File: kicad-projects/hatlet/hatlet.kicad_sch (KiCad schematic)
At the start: 46 parts, among them J1 USB Header, J2 SWD, J3 PMOD0, J4 PMOD2, J5 PMOD1, J6 UART0, J7 PMOD3, SW1 BOOTSEL, U1 AMS1117-3.3, U2 RP2040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

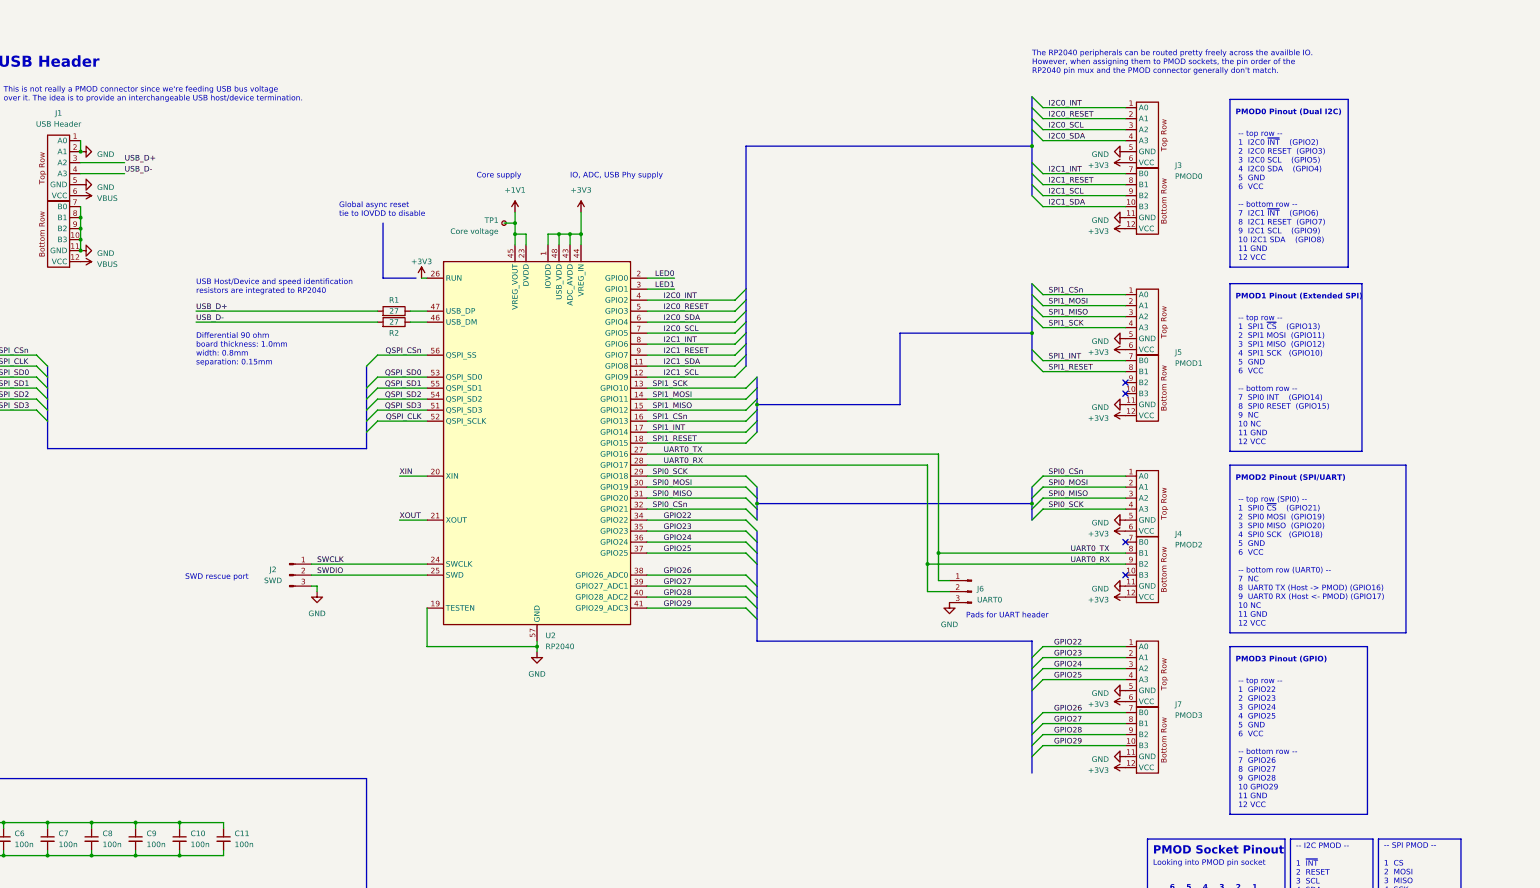
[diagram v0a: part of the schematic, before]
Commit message: Finish hatlet rev A layout
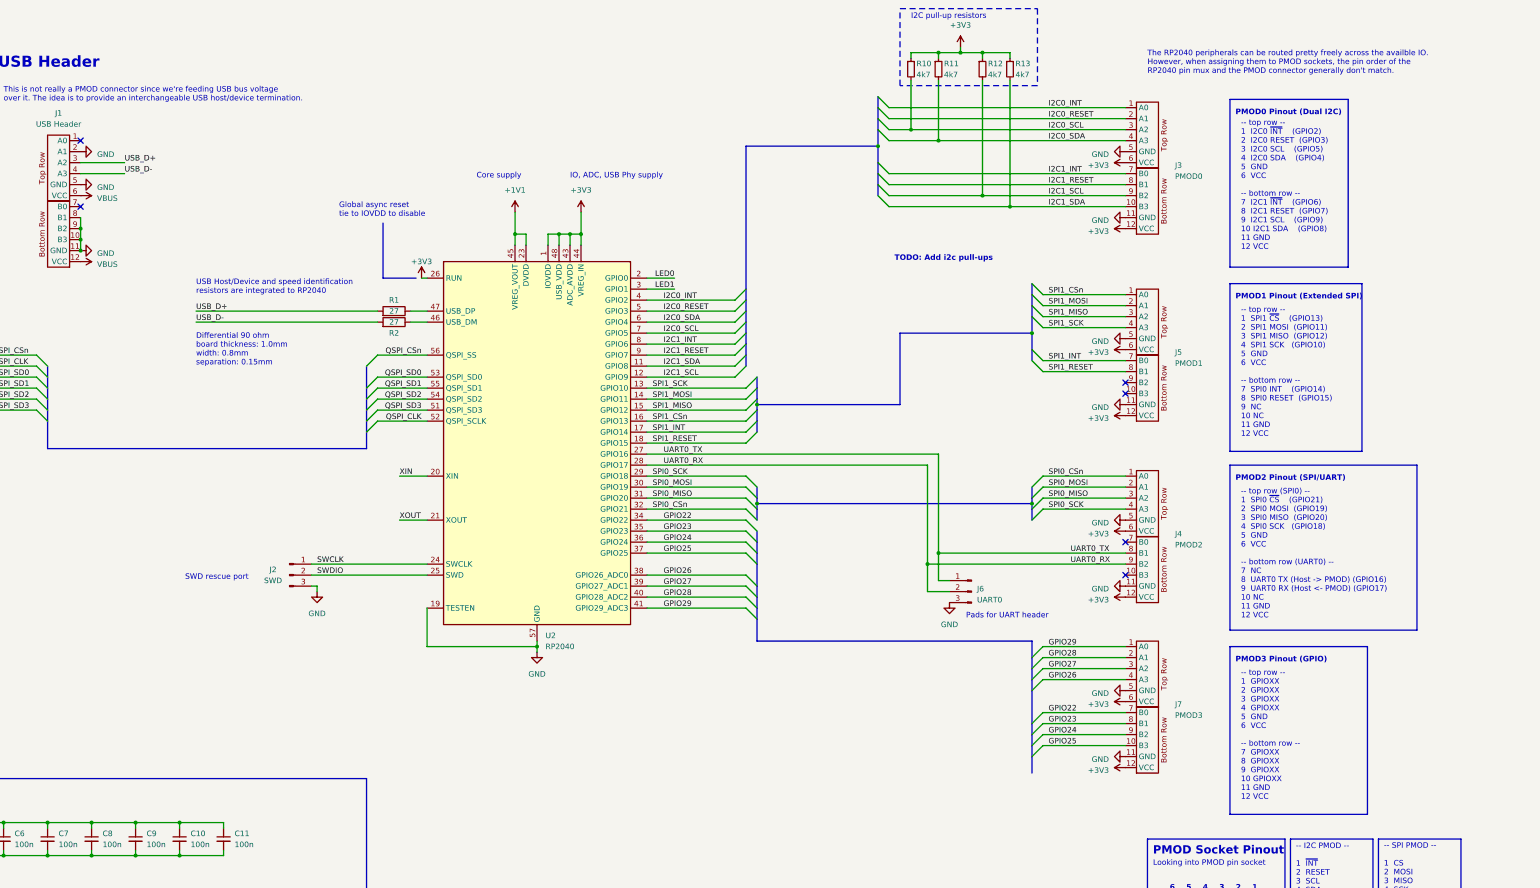
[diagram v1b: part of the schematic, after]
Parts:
- removed TP1: Core voltage, TestPoint:TestPoint_Pad_D1.0mm, symbol Connector:TestPoint_Small
- added R10, R11, R12, R13: 4k7, Resistor_SMD:R_0603_1608Metric, symbol Device:R_Small
- D1, D2, D3, D4: footprint LED_SMD:LED_0603_1608Metric -> LED_SMD:LED_0805_2012Metric
- J2, J6: footprint Connector_PinHeader_2.54mm:PinHeader_1x03_P2.54mm_Vertical -> Connector_PinHeader_2.54mm:PinHeader_1x03_P2.54mm_Horizontal
- U2: footprint Package_DFN_QFN:QFN-56-1EP_7x7mm_P0.4mm_EP3.2x3.2mm -> Package_DFN_QFN:QFN-56-1EP_7x7mm_P0.4mm_EP3.2x3.2mm_ThermalVias
- U3: footprint Package_SO:SOIC-8_5.23x5.23mm_P1.27mm -> Package_SO:SOIC-8_5.275x5.275mm_P1.27mm; lcsc (none) -> https://www.lcsc.com/product-detail/NOR-FLASH_Winbond-Elec-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
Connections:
- net +3V3: now also R10.1, R11.1, R12.1, R13.1
- net GND: no longer J1.1 (A0), J1.7 (B0)
- net GPIO22: now also J7.7 (B0); no longer J7.1 (A0)
- net GPIO23: now also J7.8 (B1); no longer J7.2 (A1)
- net GPIO24: now also J7.9 (B2); no longer J7.3 (A2)
- net GPIO25: now also J7.10 (B3); no longer J7.4 (A3)
- net GPIO26: now also J7.4 (A3); no longer J7.7 (B0)
- net GPIO27: now also J7.3 (A2); no longer J7.8 (B1)
- net GPIO28: now also J7.2 (A1); no longer J7.9 (B2)
- net GPIO29: now also J7.1 (A0); no longer J7.10 (B3)
- net I2C0_SCL: now also R10.2
- net I2C0_SDA: now also R11.2
- net I2C1_SCL: now also R12.2
- net I2C1_SDA: now also R13.2
- no-connect marks 4 -> 6
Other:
- note added: "-- top row -- 1 GPIOXX 2 GPIOXX 3 GPIOXX 4 GPIOXX 5 GND 6 VCC -- bottom row -- 7 GPIOXX 8 GPIOXX 9 GPIOXX 10 GPIOXX 11 GND 12 VCC"
- note added: "I2C pull-up resistors"
- note added: "TODO: Add i2c pull-ups"
- note removed: "-- top row -- 1 GPIO22 2 GPIO23 3 GPIO24 4 GPIO25 5 GND 6 VCC -- bottom row -- 7 GPIO26 8 GPIO27 9 GPIO28 10 GPIO29 11 GND 12 VCC"

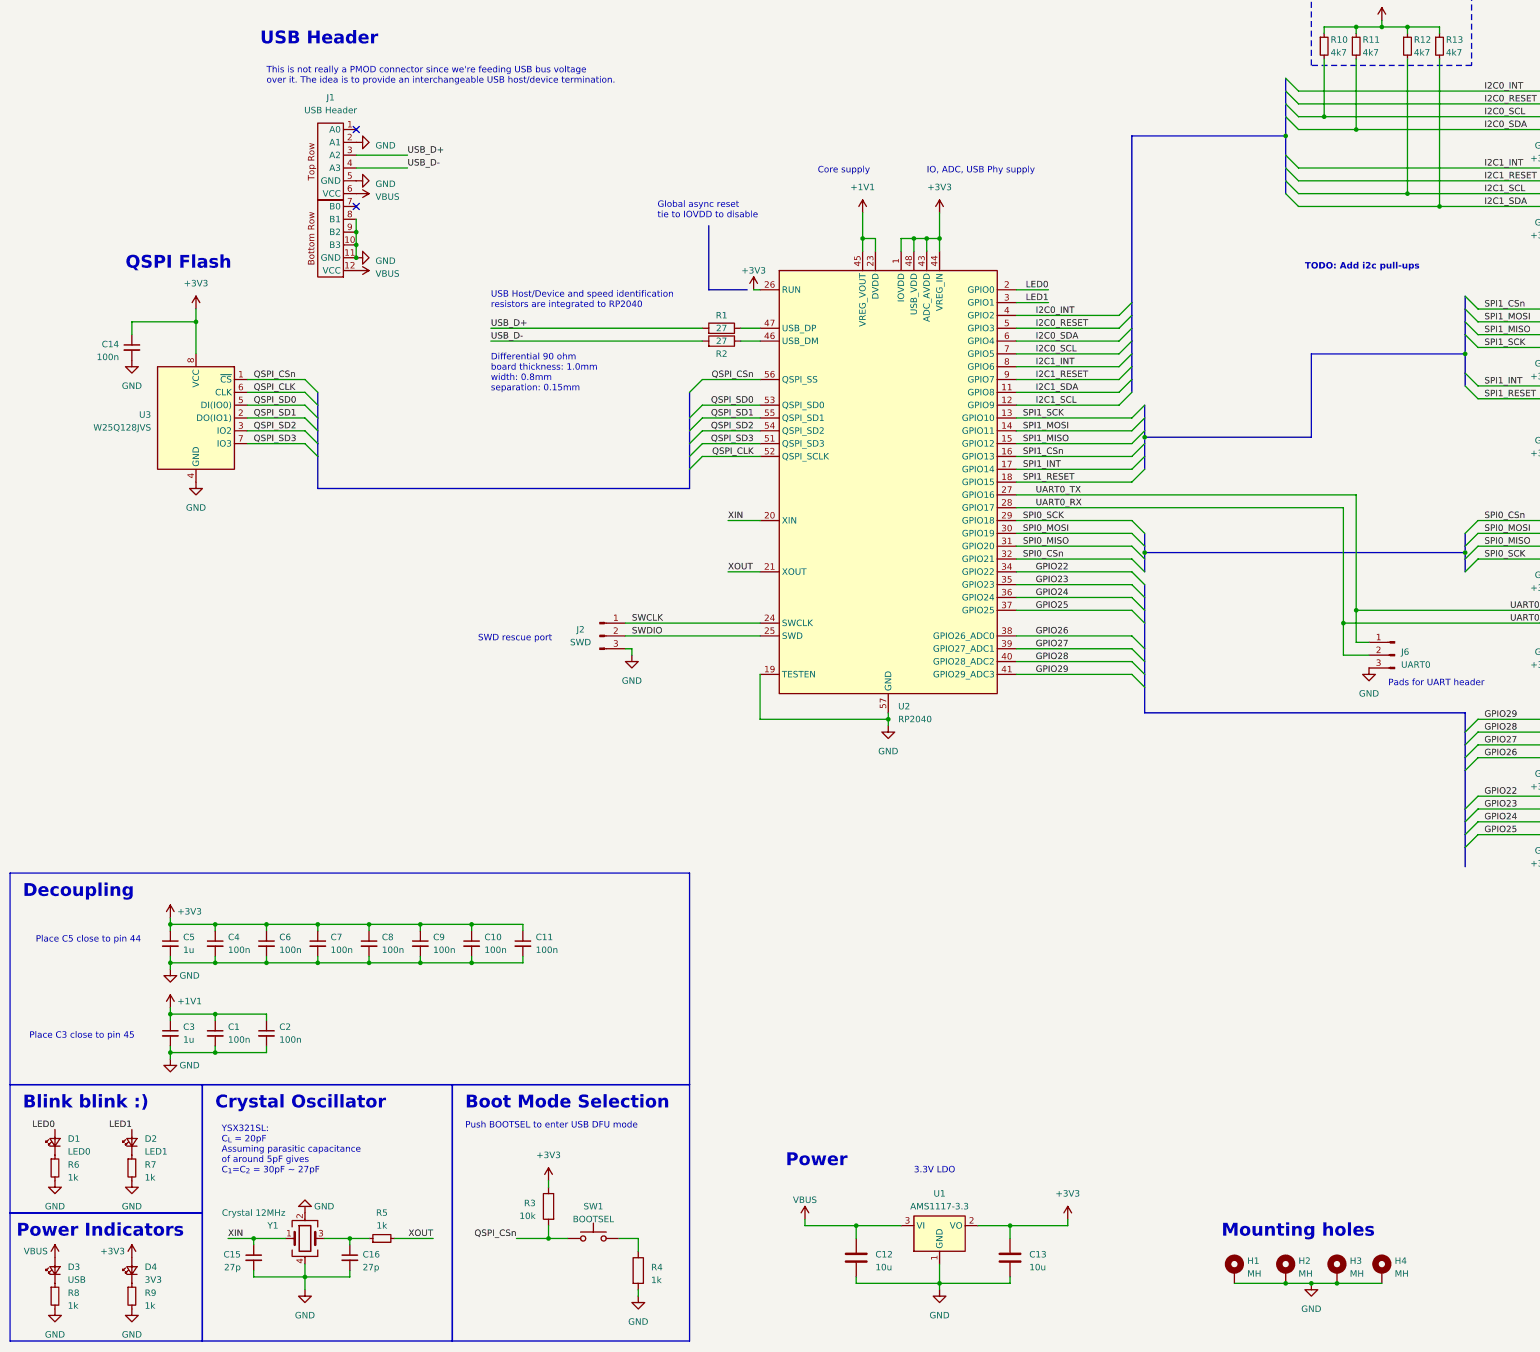
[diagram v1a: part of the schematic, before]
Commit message: Update USB header footprint
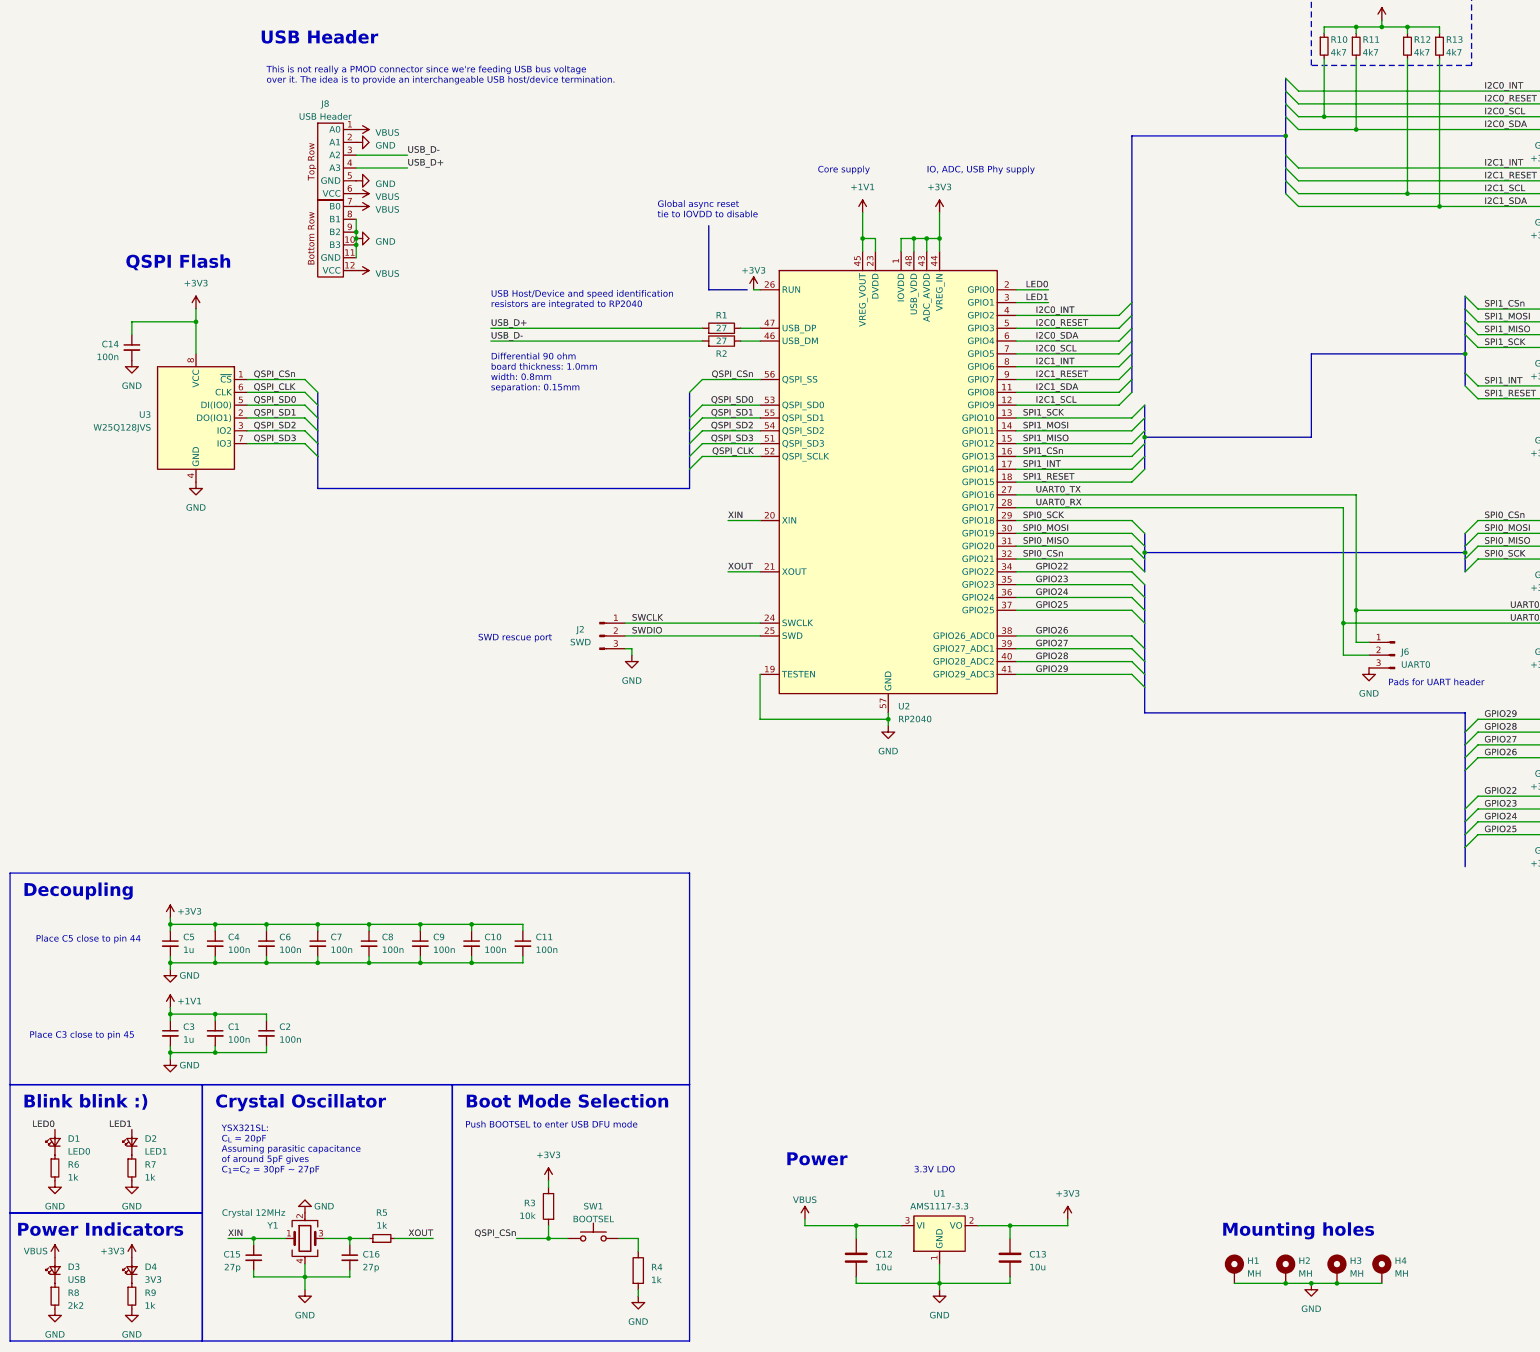
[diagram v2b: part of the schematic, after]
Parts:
- removed J1: USB Header, pmod:PMOD_PinSocket_2x06_P2.54mm_Horizontal, symbol pmod:PMOD_Host_Conn_02x06
- added J8: USB Header, racklet:Racklet_USBHeader_02x06, symbol pmod:PMOD_Peripheral_Conn_02x06
- C1, C10, C11, C14, C2, C4, C6, C7, C8, C9: JLCPCB Part # (none) -> C14663
- C12, C13: JLCPCB Part # (none) -> C96446
- C15, C16: JLCPCB Part # (none) -> C107045
- C3, C5: JLCPCB Part # (none) -> C15849
- D1, D2, D3, D4: JLCPCB Part # (none) -> C84256
- R1, R2: JLCPCB Part # (none) -> C25190
- R10, R11, R12, R13: JLCPCB Part # (none) -> C23162
- R3: JLCPCB Part # (none) -> C25804
- R4, R5, R6, R7, R9: JLCPCB Part # (none) -> C21190
- R8: value 1k -> 2k2; JLCPCB Part # (none) -> C4190
- SW1: footprint Button_Switch_SMD:SW_SPST_SKQG_WithStem -> Button_Switch_SMD:SW_SPST_TL3342; JLCPCB Part # (none) -> C318884
- U1: JLCPCB Part # (none) -> C6186
- U2: JLCPCB Part # (none) -> C2040
- U3: JLCPCB Part # (none) -> C97521
- Y1: JLCPCB Part # (none) -> C9002
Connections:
- net GND: now also J8.10 (B3), J8.11 (GND), J8.2 (A1), J8.5 (GND), J8.8 (B1), J8.9 (B2)
- net USB_D+: now also J8.4 (A3)
- net USB_D-: now also J8.3 (A2)
- net VBUS: now also J8.1 (A0), J8.12 (VCC), J8.6 (VCC), J8.7 (B0)
- no-connect marks 6 -> 4
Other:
- note removed: "TODO: Add i2c pull-ups"

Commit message: Rename schematic LCSC designator field
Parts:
- C1, C10, C11, C14, C2, C4, C6, C7, C8, C9: JLCPCB Part # C14663 -> (none); LCSC Part # (none) -> C14663
- C12, C13: JLCPCB Part # C96446 -> (none); LCSC Part # (none) -> C96446
- C15, C16: JLCPCB Part # C107045 -> (none); LCSC Part # (none) -> C107045
- C3, C5: JLCPCB Part # C15849 -> (none); LCSC Part # (none) -> C15849
- D1, D2, D3, D4: JLCPCB Part # C84256 -> (none); LCSC Part # (none) -> C84256
- R1, R2: JLCPCB Part # C25190 -> (none); LCSC Part # (none) -> C25190
- R10, R11, R12, R13: JLCPCB Part # C23162 -> (none); LCSC Part # (none) -> C23162
- R3: JLCPCB Part # C25804 -> (none); LCSC Part # (none) -> C25804
- R4, R5, R6, R7, R9: JLCPCB Part # C21190 -> (none); LCSC Part # (none) -> C21190
- R8: JLCPCB Part # C4190 -> (none); LCSC Part # (none) -> C4190
- SW1: JLCPCB Part # C318884 -> (none); LCSC Part # (none) -> C318884; lcsc https://www.lcsc.com/product-detail/Tactile-Switches_G-Swit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 -> (none)
- U1: JLCPCB Part # C6186 -> (none); LCSC Part # (none) -> C6186
- U2: JLCPCB Part # C2040 -> (none); LCSC Part # (none) -> C2040
- U3: JLCPCB Part # C97521 -> (none); LCSC Part # (none) -> C97521; lcsc https://www.lcsc.com/product-detail/NOR-FLASH_Winbond-Elec-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 -> (none)
- Y1: JLCPCB Part # C9002 -> (none); LCSC Part # (none) -> C9002; lcsc https://www.lcsc.com/product-detail/Crystals_Yangxing-Tech-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 -> (none)

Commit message: Revert "Rename schematic LCSC designator field"
This reverts commit 4d53cd782a2a552dfcb1ecbf5aa636fd93ad1774.
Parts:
- C1, C10, C11, C14, C2, C4, C6, C7, C8, C9: JLCPCB Part # (none) -> C14663; LCSC Part # C14663 -> (none)
- C12, C13: JLCPCB Part # (none) -> C96446; LCSC Part # C96446 -> (none)
- C15, C16: JLCPCB Part # (none) -> C107045; LCSC Part # C107045 -> (none)
- C3, C5: JLCPCB Part # (none) -> C15849; LCSC Part # C15849 -> (none)
- D1, D2, D3, D4: JLCPCB Part # (none) -> C84256; LCSC Part # C84256 -> (none)
- R1, R2: JLCPCB Part # (none) -> C25190; LCSC Part # C25190 -> (none)
- R10, R11, R12, R13: JLCPCB Part # (none) -> C23162; LCSC Part # C23162 -> (none)
- R3: JLCPCB Part # (none) -> C25804; LCSC Part # C25804 -> (none)
- R4, R5, R6, R7, R9: JLCPCB Part # (none) -> C21190; LCSC Part # C21190 -> (none)
- R8: JLCPCB Part # (none) -> C4190; LCSC Part # C4190 -> (none)
- SW1: JLCPCB Part # (none) -> C318884; LCSC Part # C318884 -> (none); lcsc (none) -> https://www.lcsc.com/product-detail/Tactile-Switches_G-Swit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
- U1: JLCPCB Part # (none) -> C6186; LCSC Part # C6186 -> (none)
- U2: JLCPCB Part # (none) -> C2040; LCSC Part # C2040 -> (none)
- U3: JLCPCB Part # (none) -> C97521; LCSC Part # C97521 -> (none); lcsc (none) -> https://www.lcsc.com/product-detail/NOR-FLASH_Winbond-Elec-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
- Y1: JLCPCB Part # (none) -> C9002; LCSC Part # C9002 -> (none); lcsc (none) -> https://www.lcsc.com/product-detail/Crystals_Yangxing-Tech-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

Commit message: Space out traces to reduce crosstalk
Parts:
- J3, J4, J5, J7: JLCPCB Part # (none) -> C2897426
- SW1: lcsc https://www.lcsc.com/product-detail/Tactile-Switches_G-Swit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 -> (none)
- U3: lcsc https://www.lcsc.com/product-detail/NOR-FLASH_Winbond-Elec-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 -> (none)
- Y1: lcsc https://www.lcsc.com/product-detail/Crystals_Yangxing-Tech-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 -> (none)
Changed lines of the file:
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@@
       (effects (font (size 1.27 1.27)) hide)
     )
-    (property "JLCPCB Part #" "" (at 327.66 135.89 0)
+    (property "JLCPCB Part #" "C2897426" (at 327.66 135.89 0)
       (effects (font (size 1.27 1.27)) hide)
     )
@@
       (effects (font (size 1.27 1.27)) hide)
     )
-    (property "lcsc" "https://www.lcsc.com/product-detail/Crystals_Yangxing-Tech-X322512MSB4SI_C9002.html" (at 71.12 264.16 0)
-      (effects (font (size 1.27 1.27)) hide)
-    )
     (property "JLCPCB Part #" "C9002" (at 71.12 264.16 0)
       (effects (font (size 1.27 1.27)) hide)
@@
       (effects (font (size 1.27 1.27)) hide)
     )
-    (property "JLCPCB Part #" "" (at 327.66 93.98 0)
+    (property "JLCPCB Part #" "C2897426" (at 327.66 93.98 0)
       (effects (font (size 1.27 1.27)) hide)
     )
@@
       (effects (font (size 1.27 1.27)) hide)
     )
-    (property "JLCPCB Part #" "" (at 327.66 175.26 0)
+    (property "JLCPCB Part #" "C2897426" (at 327.66 175.26 0)
       (effects (font (size 1.27 1.27)) hide)
     )
@@
       (effects (font (size 1.27 1.27)) hide)
     )
-    (property "lcsc" "https://www.lcsc.com/product-detail/Tactile-Switches_G-Switch-GT-TC084C-H015-L5_C2762971.html" (at 128.27 264.16 0)
-      (effects (font (size 1.27 1.27)) hide)
-    )
     (property "JLCPCB Part #" "C318884" (at 128.27 264.16 0)
       (effects (font (size 1.27 1.27)) hide)
@@
     )
     (property "Datasheet" "http://www.winbond.com/resource-files/w25q128jv_dtr%20revc%2003272018%20plus.pdf" (at 49.53 101.6 0)
-      (effects (font (size 1.27 1.27)) hide)
-    )
-    (property "lcsc" "https://www.lcsc.com/product-detail/NOR-FLASH_Winbond-Elec-W25Q128JVSIQ_C97521.html" (at 49.53 101.6 0)
       (effects (font (size 1.27 1.27)) hide)
     )
@@
       (effects (font (size 1.27 1.27)) hide)
     )
-    (property "JLCPCB Part #" "" (at 327.66 50.8 0)
-      (effects (font (size 1.27 1.27)) hide)
-    )
+    (property "JLCPCB Part #" "C2897426" (at 327.66 50.8 0)
+      (effects (font (size 1.27 1.27)) hide)
+    )
